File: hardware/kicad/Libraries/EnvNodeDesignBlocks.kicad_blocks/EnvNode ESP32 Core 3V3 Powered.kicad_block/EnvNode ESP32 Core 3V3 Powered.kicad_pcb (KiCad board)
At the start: 2 copper layers, 2 parts, among them U2 ESP32-DevKitC, U3 24AA025E-OT

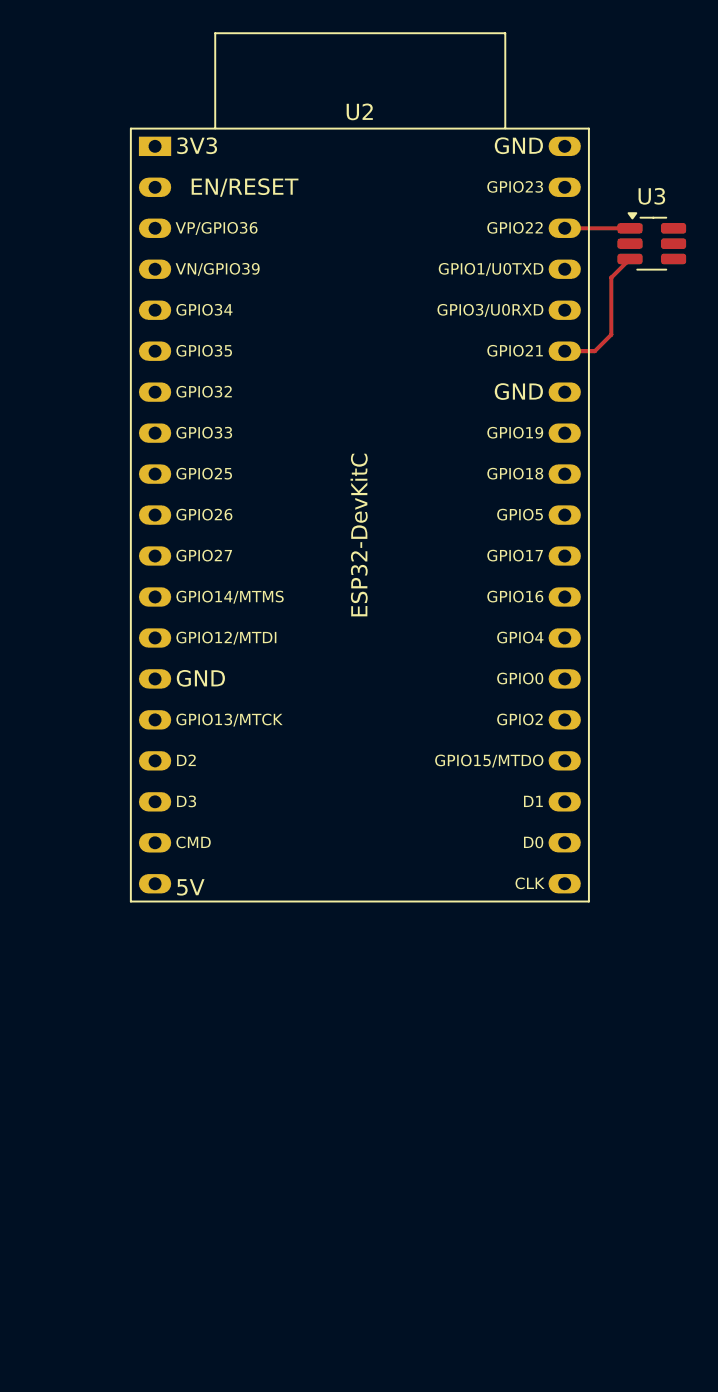
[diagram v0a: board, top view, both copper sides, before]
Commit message: DesignBlocks for ESP32 Core
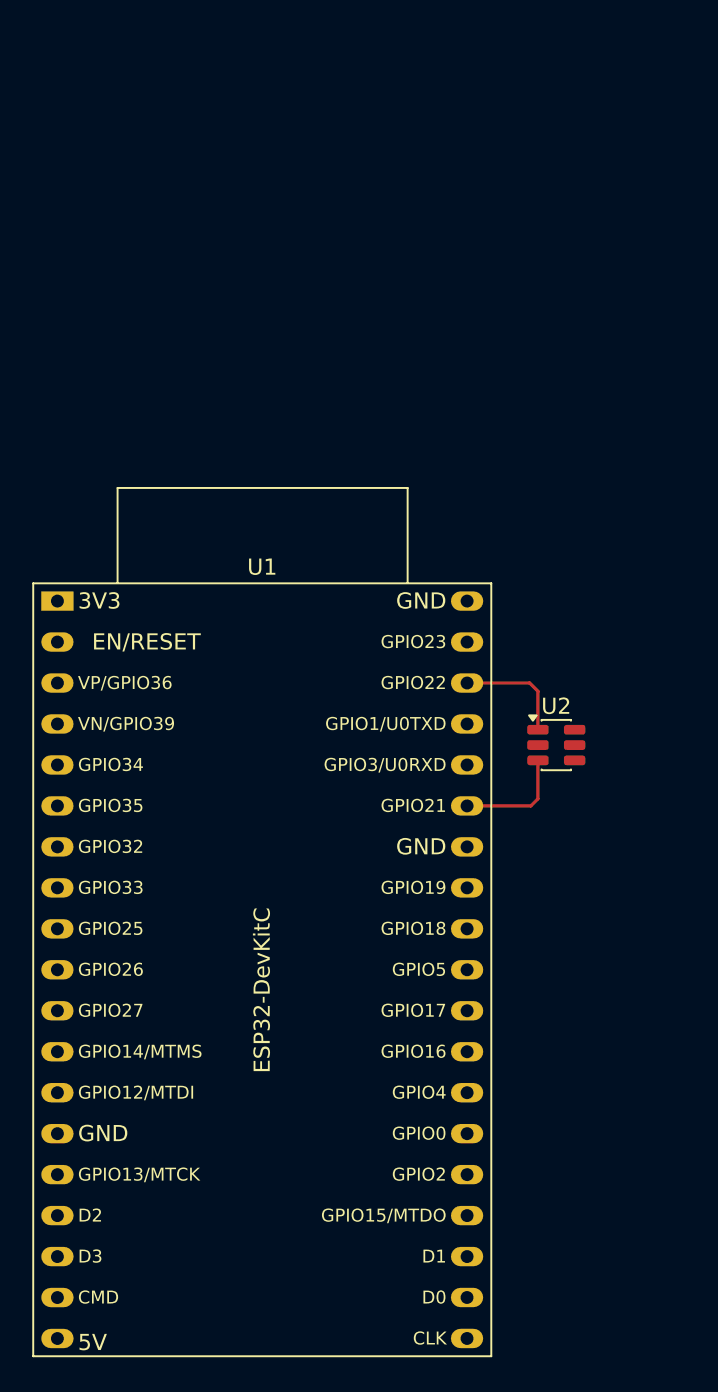
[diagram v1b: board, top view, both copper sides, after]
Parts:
- removed U3: 24AA025E-OT, Package_TO_SOT_SMD:SOT-23-6_Handsoldering
- added U1: ESP32-DevKitC, PCM_Espressif:ESP32-DevKitC, F.Cu at (109.1, 73.3)
- U2: value ESP32-DevKitC -> 24AA025E-OT; footprint PCM_Espressif:ESP32-DevKitC -> Package_TO_SOT_SMD:SOT-23-6
- moved U2 44.7 mm to (140.0, 82.2)
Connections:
- U2 pad 1: unconnected-(U2-3V3-Pad1) -> I2C0_SCL
- U2 pad 2: unconnected-(U2-CHIP_PU-Pad2) -> GND
- U2 pad 3: GPIO36 -> I2C0_SDA
- U2 pad 4: GPIO39 -> GND
- U2 pad 5: GPIO34 -> GND
- U2 pad 6: GPIO35 -> 3V3
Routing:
- net I2C0_SCL: track 4.04 -> 6.99 mm
- net I2C0_SDA: track 8.48 -> 6.96 mm
